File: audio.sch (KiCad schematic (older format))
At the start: 25 parts, among them J1401 CTIA / AHJ, U1401 SGTL5000

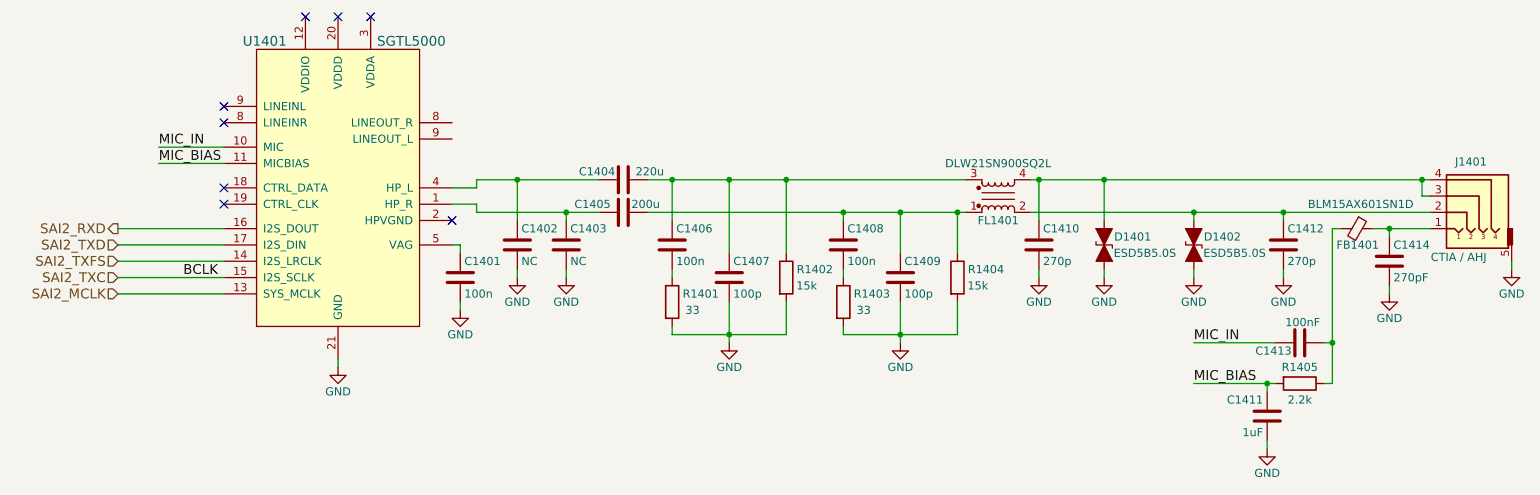
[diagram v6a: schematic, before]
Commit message: Add USB type C circuit with DRP PD capability, should sink near 2A @ 5-6.5V and source 550mA @ 5V
Removed the reverse current protection circuit from the last commit due to the requirement changing to only 18650 battery and USB-C being possible power sources

Next thing to add is the charging circuit when the USB-C is in sink mode/role
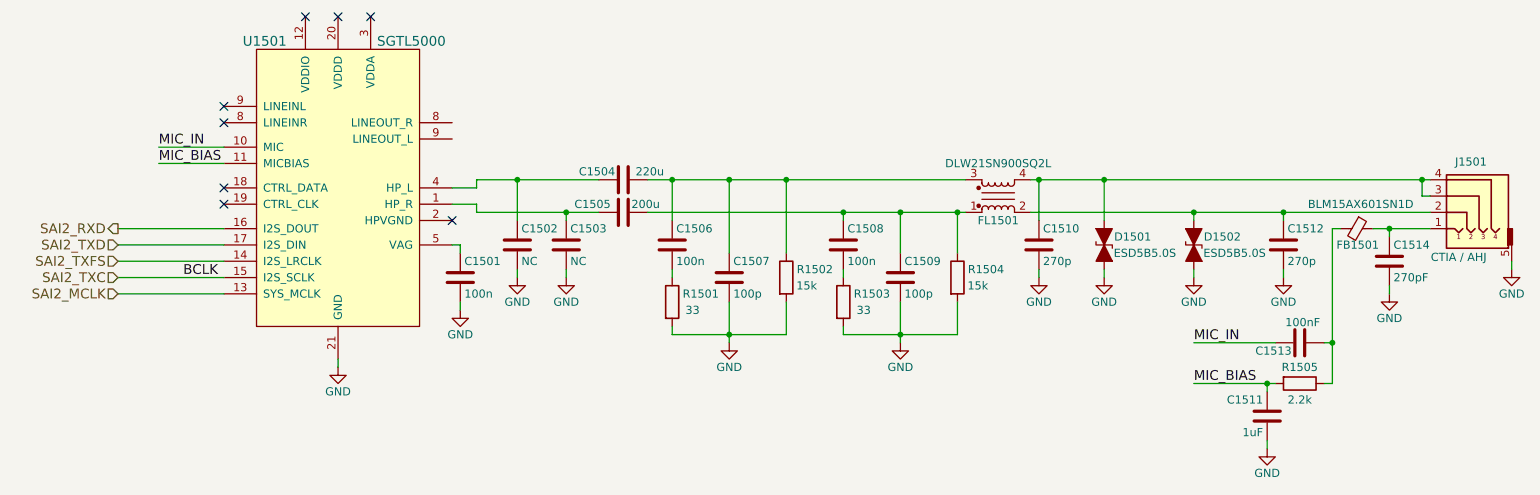
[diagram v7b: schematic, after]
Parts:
- renumbered C1401 to C1501, C1402 to C1502, C1403 to C1503, C1404 to C1504, C1405 to C1505, C1406 to C1506, C1407 to C1507, C1408 to C1508, C1409 to C1509, C1410 to C1510, C1411 to C1511, C1412 to C1512, C1413 to C1513, C1414 to C1514, D1401 to D1501, D1402 to D1502, FB1401 to FB1501, FL1401 to FL1501, J1401 to J1501, R1401 to R1501, R1402 to R1502, R1403 to R1503, R1404 to R1504, R1405 to R1505, U1401 to U1501
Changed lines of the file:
@@
 $Descr A4 11693 8268
 encoding utf-8
-Sheet 14 14
+Sheet 15 15
 Title "Audio"
-Date "2018-04-18"
+Date "2018-04-19"
 Rev "v0.1.0"
 Comp "Purism SPC"
@@
 $EndDescr
 $Comp
-L SGTL5000 U1401
+L SGTL5000 U1501
 U 1 1 5ABE7D8D
 P 3050 3350
-F 0 "U1401" H 2600 4250 60  0000 C CNN
+F 0 "U1501" H 2600 4250 60  0000 C CNN
 F 1 "SGTL5000" H 3500 4250 60  0000 C CNN
 F 2 "" H 3050 3400 60  0000 C CNN
@@
 $EndComp
 $Comp
-L GND #PWR0191
+L GND #PWR0222
 U 1 1 5ABE80CA
 P 3050 4450
-F 0 "#PWR0191" H 3050 4200 50  0001 C CNN
+F 0 "#PWR0222" H 3050 4200 50  0001 C CNN
 F 1 "GND" H 3050 4300 50  0000 C CNN
 F 2 "" H 3050 4450 50  0001 C CNN
@@
 	1700 3900 2350 3900
 $Comp
-L C C1404
+L C C1504
 U 1 1 5ABEEF4C
 P 4800 3300
-F 0 "C1404" V 4850 3350 50  0000 L CNN
+F 0 "C1504" V 4850 3350 50  0000 L CNN
 F 1 "220u" V 4850 3050 50  0000 L CNN
 F 2 "" H 4838 3150 50  0001 C CNN
@@
 $EndComp
 $Comp
-L C C1405
+L C C1505
 U 1 1 5ABEEF73
 P 4800 3500
-F 0 "C1405" V 4850 3200 50  0000 L CNN
+F 0 "C1505" V 4850 3200 50  0000 L CNN
 F 1 "200u" V 4850 3550 50  0000 L CNN
 F 2 "" H 4838 3350 50  0001 C CNN
@@
 	3900 3500 4650 3500
 $Comp
-L C C1402
+L C C1502
 U 1 1 5ABEF358
 P 4150 3700
-F 0 "C1402" H 4175 3800 50  0000 L CNN
+F 0 "C1502" H 4175 3800 50  0000 L CNN
 F 1 "NC" H 4175 3600 50  0000 L CNN
 F 2 "" H 4188 3550 50  0001 C CNN
@@
 $EndComp
 $Comp
-L C C1403
+L C C1503
 U 1 1 5ABEF388
 P 4450 3700
-F 0 "C1403" H 4475 3800 50  0000 L CNN
+F 0 "C1503" H 4475 3800 50  0000 L CNN
 F 1 "NC" H 4475 3600 50  0000 L CNN
 F 2 "" H 4488 3550 50  0001 C CNN
@@
 $EndComp
 $Comp
-L GND #PWR0192
+L GND #PWR0223
 U 1 1 5ABEF777
 P 4450 3900
-F 0 "#PWR0192" H 4450 3650 50  0001 C CNN
+F 0 "#PWR0223" H 4450 3650 50  0001 C CNN
 F 1 "GND" H 4450 3750 50  0000 C CNN
 F 2 "" H 4450 3900 50  0001 C CNN
@@
 $EndComp
 $Comp
-L GND #PWR0193
+L GND #PWR0224
 U 1 1 5ABEF798
 P 4150 3900
-F 0 "#PWR0193" H 4150 3650 50  0001 C CNN
+F 0 "#PWR0224" H 4150 3650 50  0001 C CNN
 F 1 "GND" H 4150 3750 50  0000 C CNN
 F 2 "" H 4150 3900 50  0001 C CNN
@@
 	4150 3850 4150 3900
 $Comp
-L R R1401
+L R R1501
 U 1 1 5ABEFC7B
 P 5100 4050
-F 0 "R1401" H 5275 4100 50  0000 C CNN
+F 0 "R1501" H 5275 4100 50  0000 C CNN
 F 1 "33" H 5225 4000 50  0000 C CNN
 F 2 "" V 5030 4050 50  0001 C CNN
@@
 	5100 3850 5100 3900
 $Comp
-L GND #PWR0194
+L GND #PWR0225
 U 1 1 5ABF0047
 P 5450 4300
-F 0 "#PWR0194" H 5450 4050 50  0001 C CNN
+F 0 "#PWR0225" H 5450 4050 50  0001 C CNN
 F 1 "GND" H 5450 4150 50  0000 C CNN
 F 2 "" H 5450 4300 50  0001 C CNN
@@
 	5100 4200 5100 4250
 $Comp
-L EMI_Filter_CommonMode FL1401
+L EMI_Filter_CommonMode FL1501
 U 1 1 5ABF2412
 P 7100 3400
-F 0 "FL1401" H 7100 3550 50  0000 C CNN
+F 0 "FL1501" H 7100 3550 50  0000 C CNN
 F 1 "DLW21SN900SQ2L" H 7100 3200 50  0000 C CNN
 F 2 "" V 7100 3440 50  0000 C CNN
@@
 $EndComp
 $Comp
-L C C1412
+L C C1512
 U 1 1 5ABF2943
 P 8850 3700
-F 0 "C1412" H 8875 3800 50  0000 L CNN
+F 0 "C1512" H 8875 3800 50  0000 L CNN
 F 1 "270p" H 8875 3600 50  0000 L CNN
 F 2 "" H 8888 3550 50  0001 C CNN
@@
 $EndComp
 $Comp
-L C C1410
+L C C1510
 U 1 1 5ABF2987
 P 7350 3700
-F 0 "C1410" H 7375 3800 50  0000 L CNN
+F 0 "C1510" H 7375 3800 50  0000 L CNN
 F 1 "270p" H 7375 3600 50  0000 L CNN
 F 2 "" H 7388 3550 50  0001 C CNN
@@
 	8850 3500 8850 3550
 $Comp
-L GND #PWR0195
+L GND #PWR0226
 U 1 1 5ABF2BDF
 P 8850 3900
-F 0 "#PWR0195" H 8850 3650 50  0001 C CNN
+F 0 "#PWR0226" H 8850 3650 50  0001 C CNN
 F 1 "GND" H 8850 3750 50  0000 C CNN
 F 2 "" H 8850 3900 50  0001 C CNN
@@
 	8850 3900 8850 3850
 $Comp
-L GND #PWR0196
+L GND #PWR0227
 U 1 1 5ABF2C32
 P 7350 3900
-F 0 "#PWR0196" H 7350 3650 50  0001 C CNN
+F 0 "#PWR0227" H 7350 3650 50  0001 C CNN
 F 1 "GND" H 7350 3750 50  0000 C CNN
 F 2 "" H 7350 3900 50  0001 C CNN
@@
 Connection ~ 4150 3300
 $Comp
-L C C1406
+L C C1506
 U 1 1 5ABF4002
 P 5100 3700
-F 0 "C1406" H 5125 3800 50  0000 L CNN
+F 0 "C1506" H 5125 3800 50  0000 L CNN
 F 1 "100n" H 5125 3600 50  0000 L CNN
 F 2 "" H 5138 3550 50  0001 C CNN
@@
 $EndComp
 $Comp
-L C C1407
+L C C1507
 U 1 1 5ABF490A
 P 5450 3900
-F 0 "C1407" H 5475 4000 50  0000 L CNN
+F 0 "C1507" H 5475 4000 50  0000 L CNN
 F 1 "100p" H 5475 3800 50  0000 L CNN
 F 2 "" H 5488 3750 50  0001 C CNN
@@
 $EndComp
 $Comp
-L R R1402
+L R R1502
 U 1 1 5ABF49BF
 P 5800 3900
-F 0 "R1402" H 5975 3950 50  0000 C CNN
+F 0 "R1502" H 5975 3950 50  0000 C CNN
 F 1 "15k" H 5925 3850 50  0000 C CNN
 F 2 "" V 5730 3900 50  0001 C CNN
@@
 Connection ~ 5800 3300
 $Comp
-L R R1403
+L R R1503
 U 1 1 5ABF53AE
 P 6150 4050
-F 0 "R1403" H 6325 4100 50  0000 C CNN
+F 0 "R1503" H 6325 4100 50  0000 C CNN
 F 1 "33" H 6275 4000 50  0000 C CNN
 F 2 "" V 6080 4050 50  0001 C CNN
@@
 	6150 3850 6150 3900
 $Comp
-L GND #PWR0197
+L GND #PWR0228
 U 1 1 5ABF53B5
 P 6500 4300
-F 0 "#PWR0197" H 6500 4050 50  0001 C CNN
+F 0 "#PWR0228" H 6500 4050 50  0001 C CNN
 F 1 "GND" H 6500 4150 50  0000 C CNN
 F 2 "" H 6500 4300 50  0001 C CNN
@@
 	6150 4200 6150 4250
 $Comp
-L C C1408
+L C C1508
 U 1 1 5ABF53BC
 P 6150 3700
-F 0 "C1408" H 6175 3800 50  0000 L CNN
+F 0 "C1508" H 6175 3800 50  0000 L CNN
 F 1 "100n" H 6175 3600 50  0000 L CNN
 F 2 "" H 6188 3550 50  0001 C CNN
@@
 $EndComp
 $Comp
-L C C1409
+L C C1509
 U 1 1 5ABF53C2
 P 6500 3900
-F 0 "C1409" H 6525 4000 50  0000 L CNN
+F 0 "C1509" H 6525 4000 50  0000 L CNN
 F 1 "100p" H 6525 3800 50  0000 L CNN
 F 2 "" H 6538 3750 50  0001 C CNN
@@
 $EndComp
 $Comp
-L R R1404
+L R R1504
 U 1 1 5ABF53C8
 P 6850 3900
-F 0 "R1404" H 7025 3950 50  0000 C CNN
+F 0 "R1504" H 7025 3950 50  0000 C CNN
 F 1 "15k" H 6975 3850 50  0000 C CNN
 F 2 "" V 6780 3900 50  0001 C CNN
@@
 Connection ~ 6850 3500
 $Comp
-L D_TVS_ALT D1401
+L D_TVS_ALT D1501
 U 1 1 5ABF82C5
 P 7750 3700
-F 0 "D1401" V 7700 3875 50  0000 C CNN
+F 0 "D1501" V 7700 3875 50  0000 C CNN
 F 1 "ESD5B5.0S" V 7800 3950 50  0000 C CNN
 F 2 "" H 7750 3700 50  0001 C CNN
@@
 $EndComp
 $Comp
-L GND #PWR0198
+L GND #PWR0229
 U 1 1 5ABF847B
 P 7750 3900
-F 0 "#PWR0198" H 7750 3650 50  0001 C CNN
+F 0 "#PWR0229" H 7750 3650 50  0001 C CNN
 F 1 "GND" H 7750 3750 50  0000 C CNN
 F 2 "" H 7750 3900 50  0001 C CNN
@@
 	7750 3900 7750 3850
 $Comp
-L D_TVS_ALT D1402
+L D_TVS_ALT D1502
 U 1 1 5ABF8533
 P 8300 3700
-F 0 "D1402" V 8250 3875 50  0000 C CNN
+F 0 "D1502" V 8250 3875 50  0000 C CNN
 F 1 "ESD5B5.0S" V 8350 3950 50  0000 C CNN
 F 2 "" H 8300 3700 50  0001 C CNN
@@
 	8300 3500 8300 3550
 $Comp
-L GND #PWR0199
+L GND #PWR0230
 U 1 1 5ABF8745
 P 8300 3900
-F 0 "#PWR0199" H 8300 3650 50  0001 C CNN
+F 0 "#PWR0230" H 8300 3650 50  0001 C CNN
 F 1 "GND" H 8300 3750 50  0000 C CNN
 F 2 "" H 8300 3900 50  0001 C CNN
@@
 Connection ~ 8300 3500
 $Comp
-L Audio-Jack-5 J1401
+L Audio-Jack-5 J1501
 U 1 1 5ABF9919
 P 9950 3400
-F 0 "J1401" H 9900 3610 50  0000 C CNN
+F 0 "J1501" H 9900 3610 50  0000 C CNN
 F 1 "CTIA / AHJ" H 9975 3025 50  0000 C CNN
 F 2 "" H 10200 3500 50  0001 C CNN
@@
 Connection ~ 9700 3300
 $Comp
-L GND #PWR0200
+L GND #PWR0231
 U 1 1 5ABFAC4D
 P 10250 3850
-F 0 "#PWR0200" H 10250 3600 50  0001 C CNN
+F 0 "#PWR0231" H 10250 3600 50  0001 C CNN
 F 1 "GND" H 10250 3700 50  0000 C CNN
 F 2 "" H 10250 3850 50  0001 C CNN
@@
 MIC_IN
 $Comp
-L C C1401
+L C C1501
 U 1 1 5ABFC3EE
 P 3800 3900
-F 0 "C1401" H 3825 4000 50  0000 L CNN
+F 0 "C1501" H 3825 4000 50  0000 L CNN
 F 1 "100n" H 3825 3800 50  0000 L CNN
 F 2 "" H 3838 3750 50  0001 C CNN
@@
 $EndComp
 $Comp
-L GND #PWR0201
+L GND #PWR0232
 U 1 1 5ABFCB56
 P 3800 4100
-F 0 "#PWR0201" H 3800 3850 50  0001 C CNN
+F 0 "#PWR0232" H 3800 3850 50  0001 C CNN
 F 1 "GND" H 3800 3950 50  0000 C CNN
 F 2 "" H 3800 4100 50  0001 C CNN
@@
 NoConn ~ 3750 3550
 $Comp
-L C C1414
+L C C1514
 U 1 1 5AC79EEC
 P 9500 3800
-F 0 "C1414" H 9525 3900 50  0000 L CNN
+F 0 "C1514" H 9525 3900 50  0000 L CNN
 F 1 "270pF" H 9525 3700 50  0000 L CNN
 F 2 "" H 9538 3650 50  0001 C CNN
@@
 $EndComp
 $Comp
-L Ferrite_Bead_Small FB1401
+L Ferrite_Bead_Small FB1501
 U 1 1 5AC7A038
 P 9300 3600
-F 0 "FB1401" V 9400 3475 50  0000 L CNN
+F 0 "FB1501" V 9400 3475 50  0000 L CNN
 F 1 "BLM15AX601SN1D" V 9150 3300 50  0000 L CNN
 F 2 "" V 9230 3600 50  0001 C CNN
@@
 $EndComp
 $Comp
-L GND #PWR0202
+L GND #PWR0233
 U 1 1 5AC7A8FB
 P 9500 4000
-F 0 "#PWR0202" H 9500 3750 50  0001 C CNN
+F 0 "#PWR0233" H 9500 3750 50  0001 C CNN
 F 1 "GND" H 9500 3850 50  0000 C CNN
 F 2 "" H 9500 4000 50  0001 C CNN
@@
 	9400 3600 9750 3600
 $Comp
-L R R1405
+L R R1505
 U 1 1 5AC7B464
 P 8950 4550
-F 0 "R1405" V 8850 4550 50  0000 C CNN
+F 0 "R1505" V 8850 4550 50  0000 C CNN
 F 1 "2.2k" V 9050 4550 50  0000 C CNN
 F 2 "" V 8880 4550 50  0001 C CNN
@@
 	9150 3600 9200 3600
 $Comp
-L C C1413
+L C C1513
 U 1 1 5AC7B848
 P 8950 4300
-F 0 "C1413" V 8900 4350 50  0000 L CNN
+F 0 "C1513" V 8900 4350 50  0000 L CNN
 F 1 "100nF" V 9075 4175 50  0000 L CNN
 F 2 "" H 8988 4150 50  0001 C CNN
@@
 Connection ~ 9150 4300
 $Comp
-L C C1411
+L C C1511
 U 1 1 5AC7BC8A
 P 8750 4750
-F 0 "C1411" H 8775 4850 50  0000 L CNN
+F 0 "C1511" H 8775 4850 50  0000 L CNN
 F 1 "1uF" H 8775 4650 50  0000 L CNN
 F 2 "" H 8788 4600 50  0001 C CNN
@@
 Connection ~ 8750 4550
 $Comp
-L GND #PWR0203
+L GND #PWR0234
 U 1 1 5AC7C780
 P 8750 4950
-F 0 "#PWR0203" H 8750 4700 50  0001 C CNN
+F 0 "#PWR0234" H 8750 4700 50  0001 C CNN
 F 1 "GND" H 8750 4800 50  0000 C CNN
 F 2 "" H 8750 4950 50  0001 C CNN
